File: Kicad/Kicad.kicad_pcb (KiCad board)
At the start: 2 copper layers, 17 parts, among them J1 Screw_Terminal_01x02, J2 Screw_Terminal_01x02, J3 Screw_Terminal_01x04, J4 Conn_01x04_Pin, J5 Conn_01x04_Pin, U1 ESP32-WROOM-32, U2 DRV8833PW, U5 TSOP382xx

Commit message: Main Board v1
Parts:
- removed U1: ESP32-WROOM-32, RF_Module:ESP32-WROOM-32
- added U3: ~, ESP32_Footprints:ESP32_30pin, F.Cu at (67.5, 93.7)
- moved J4 62.9 mm to (45.7, 104.1)
- moved C4 53.5 mm to (101.6, 66.7), turned to 90 degrees
- moved J2 45.9 mm to (100.3, 90.8), turned to -90 degrees
- moved R1 41.1 mm to (90.2, 112.5), turned to -90 degrees
- moved U5 37.3 mm to (47.6, 94.0), turned to -90 degrees
- moved C3 35.0 mm to (87.0, 112.5)
- moved J1 34.3 mm to (100.4, 107.3)
- moved C7 29.9 mm to (85.7, 102.2), turned to 90 degrees
- moved J3 27.4 mm to (109.4, 82.5)
- moved U2 26.5 mm to (88.6, 97.4), turned to 180 degrees
- moved A1 26.2 mm to (97.8, 83.8)
- moved C6 23.0 mm to (90.7, 104.8)
- moved C5 23.0 mm to (90.8, 102.2)
- moved C1 18.1 mm to (48.9, 76.8)
- moved C2 18.1 mm to (51.4, 76.8)
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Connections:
- C3 pad 1: GND -> /EN
- C3 pad 2: Net-(U1-EN) -> GND
- R1 pad 2: Net-(U1-EN) -> /EN
- U2 pad 10: /IO28 -> /IO26
- U2 pad 15: /IO26 -> /IO27
- U2 pad 16: /IO25 -> /IO28
- U2 pad 9: /IO27 -> /IO25
- U5 pad 1: /IO22 -> /IO5
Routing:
- net /3v3: track 0.00 -> 137.2 mm
- net /12V: track 0.00 -> 64.4 mm
- net GND: track 0.00 -> 33.4 mm, vias 0 -> 8
- net /IO23: track 0.00 -> 28.7 mm
- net /NEMA_Output_2b: track 0.00 -> 13.2 mm
- net /NEMA_Output_1a: track 0.00 -> 13.2 mm
- net /DC_Output_1a: track 0.00 -> 13.0 mm
- net /NEMA_Output_2a: track 0.00 -> 12.1 mm
- net /NEMA_Output_1b: track 0.00 -> 12.1 mm
- net /DC_Output_2a: track 0.00 -> 11.0 mm
- net /EN: track 0.00 -> 10.8 mm
- net /DC_Output_1b: track 0.00 -> 10.8 mm
- net /DC_Output_2b: track 0.00 -> 9.39 mm
- net /IO22: track 0.00 -> 8.89 mm
- net /IO21: track 0.00 -> 8.89 mm
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- added copper zone on B.Cu, net GND
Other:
- board outline added: 74.3 x 54.6 mm

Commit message: Created cad for how the boards will fit together
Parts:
- J1, J2: footprint TerminalBlock_RND:TerminalBlock_RND_205-00232_1x02_P5.08mm_Horizontal -> TerminalBlock_RND:TerminalBlock_RND_205-00045_1x02_P5.00mm_Horizontal
- J3: footprint TerminalBlock_Phoenix:TerminalBlock_Phoenix_MKDS-3-4-5.08_1x04_P5.08mm_Horizontal -> TerminalBlock_RND:TerminalBlock_RND_205-00003_1x04_P5.00mm_Horizontal
- moved J2 5.08 mm to (100.3, 95.9), turned to 90 degrees
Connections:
- U2 pad 5: /DC_Output_2b -> /DC_Output_2a
- U2 pad 7: /DC_Output_2a -> /DC_Output_2b
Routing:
- net /DC_Output_2b: track 9.39 -> 11.0 mm
- net /DC_Output_2a: track 11.0 -> 9.39 mm

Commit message: Wrote v1 of the code, final version of boards
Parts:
- added G***: LOGO, LOGO, F.Cu at (92.6, 106.8)
- C1, C5: value 10u -> 10uF; footprint Capacitor_SMD:C_0603_1608Metric -> PCM_JLCPCB:C_0603
- C2, C3: value 0.1u -> 100nF; footprint Capacitor_SMD:C_0603_1608Metric -> PCM_JLCPCB:C_0603
- C4: footprint Capacitor_SMD:C_0603_1608Metric -> Capacitor_THT:C_Radial_D8.0mm_H11.5mm_P3.50mm
- C6: value 0.01u -> 10nF; footprint Capacitor_SMD:C_0603_1608Metric -> PCM_JLCPCB:C_0603
- C7: value 2.2u -> 2.2uF; footprint Capacitor_SMD:C_0603_1608Metric -> PCM_JLCPCB:C_0603
- R1: value 10k -> 10kΩ; footprint Resistor_SMD:R_0603_1608Metric -> PCM_JLCPCB:R_0603
- moved C4 10.1 mm to (91.5, 66.5)
- moved R1 10.1 mm to (84.8, 104.0)
- moved C3 9.61 mm to (82.5, 104.0)
- moved J4 7.57 mm to (48.0, 96.9)
- moved U5 6.99 mm to (48.0, 87.0)
- moved J5 6.98 mm to (45.7, 69.2)
- moved J2 6.91 mm to (106.5, 99.0)
- moved C1 6.85 mm to (48.5, 70.0)
- moved C2 6.83 mm to (51.4, 70.0)
- moved J1 6.79 mm to (106.4, 110.5)
- moved U3 6.52 mm to (67.1, 87.2), turned to 90 degrees
- moved A1 4.91 mm to (97.2, 88.7)
- moved C6 4.43 mm to (89.5, 100.5)
- moved C5 3.96 mm to (89.5, 98.5)
- moved C7 3.67 mm to (84.5, 98.8)
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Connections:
- U3 pad 10: /IO27 -> /IO28
- U3 pad 11: /IO28 -> unconnected-(U3-GPIO35-Pad11)
- U3 pad 6: unconnected-(U3-GPIO27-Pad6) -> /IO23
- U3 pad 7: /IO23 -> /IO25
- U3 pad 8: /IO25 -> /IO26
- U3 pad 9: /IO26 -> /IO27
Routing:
- net /3v3: track 137.2 -> 111.1 mm
- net /IO23: track 28.7 -> 15.7 mm
- net /DC_Output_1b: track 10.8 -> 20.6 mm
- net /DC_Output_1a: track 13.0 -> 22.2 mm
- net /DC_Output_2a: track 9.39 -> 18.3 mm
- net /IO18: track 5.07 -> 13.7 mm
- net /IO19: track 5.07 -> 13.7 mm
- net GND: track 33.4 -> 25.0 mm, vias 8 -> 14
- net /12V: track 64.4 -> 57.3 mm
- net /EN: track 10.8 -> 4.85 mm
- net /DC_Output_2b: track 11.0 -> 16.8 mm
- net /IO25: track 6.20 -> 9.19 mm
- net /IO27: track 5.72 -> 8.48 mm
- net /IO26: track 6.01 -> 8.35 mm
- net /IO22: track 8.89 -> 6.71 mm
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
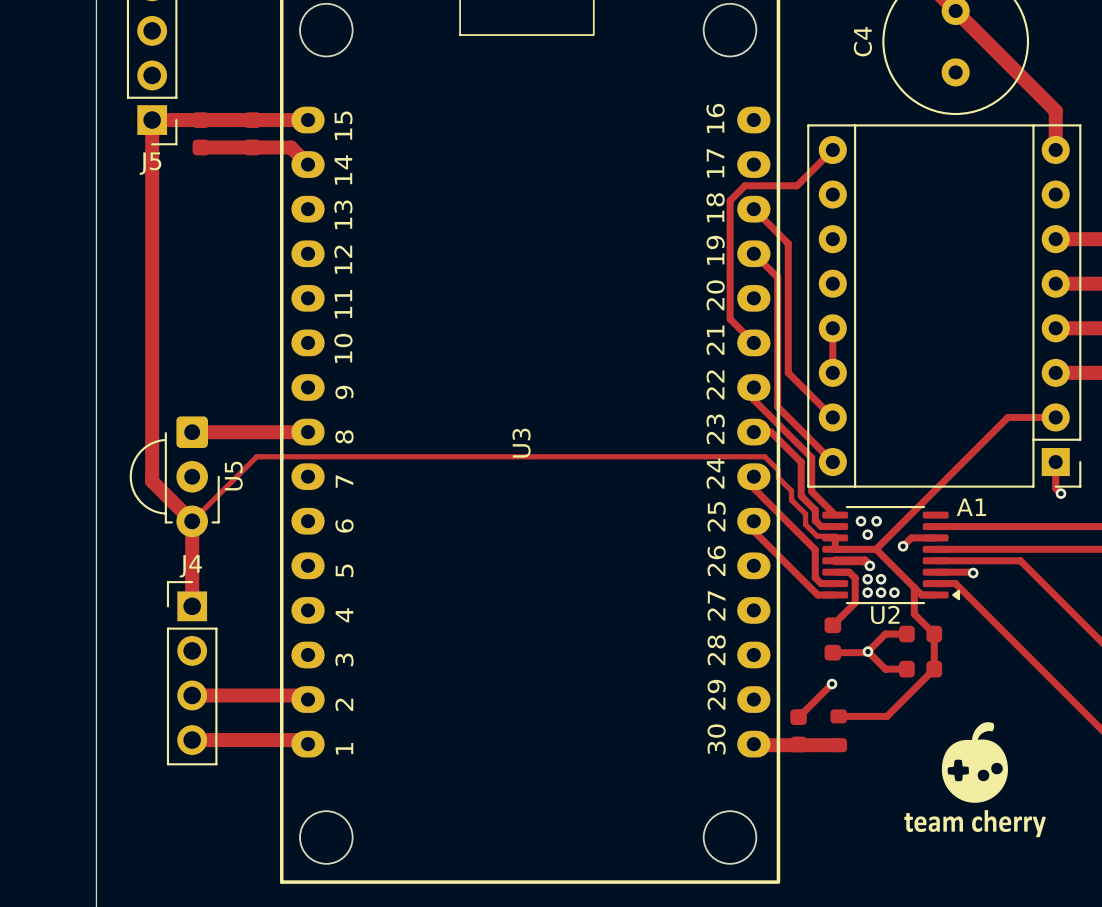
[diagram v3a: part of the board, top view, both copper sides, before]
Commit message: Updated to use 0805 instead of JLC assembly
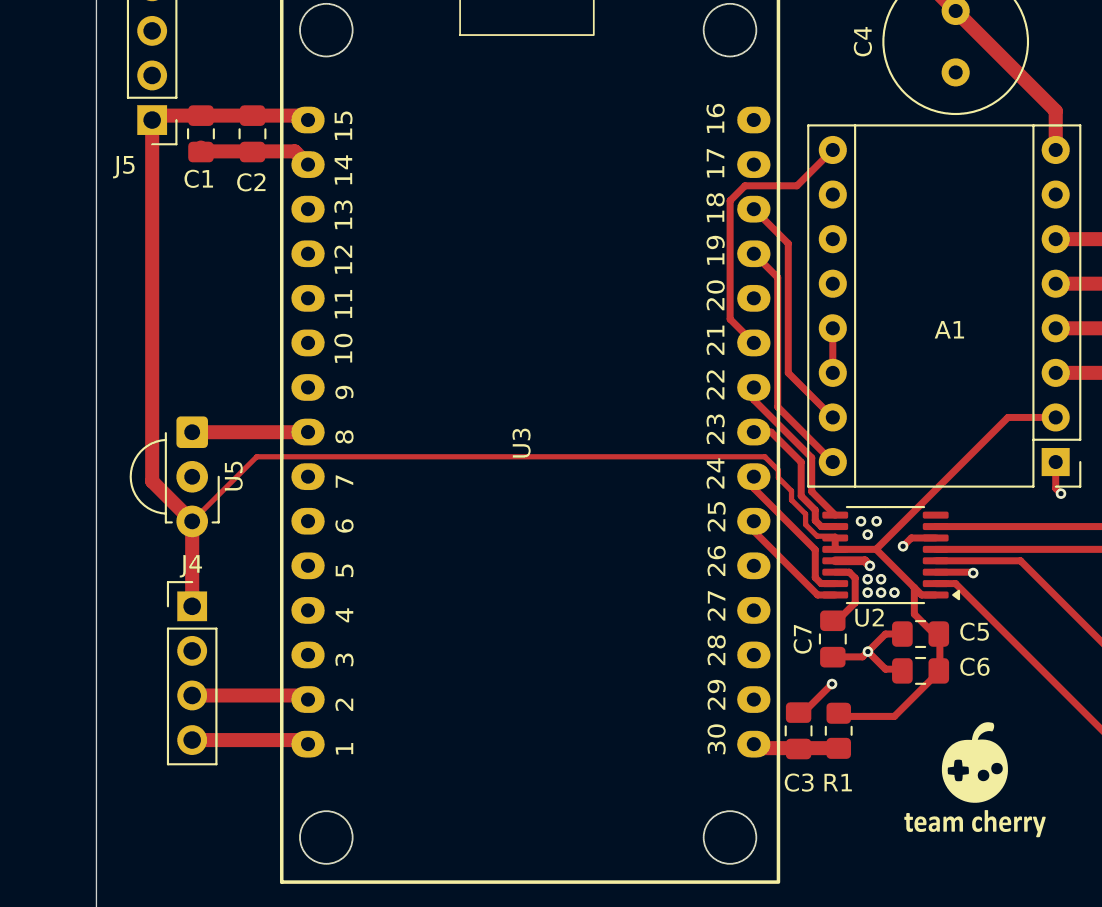
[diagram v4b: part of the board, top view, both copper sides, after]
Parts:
- C1, C2, C3, C5, C6, C7: footprint PCM_JLCPCB:C_0603 -> Capacitor_SMD:C_0805_2012Metric_Pad1.18x1.45mm_HandSolder
- R1: footprint PCM_JLCPCB:R_0603 -> Resistor_SMD:R_0805_2012Metric_Pad1.20x1.40mm_HandSolder
- moved C6 0.10 mm to (89.5, 100.6)
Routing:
- net /3v3: track 111.1 -> 111.8 mm
